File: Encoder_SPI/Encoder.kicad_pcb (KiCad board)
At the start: 2 copper layers, 21 x 17 mm, 11 parts, among them J1 Conn_01x06, J2 PWM, U1 AS5048A

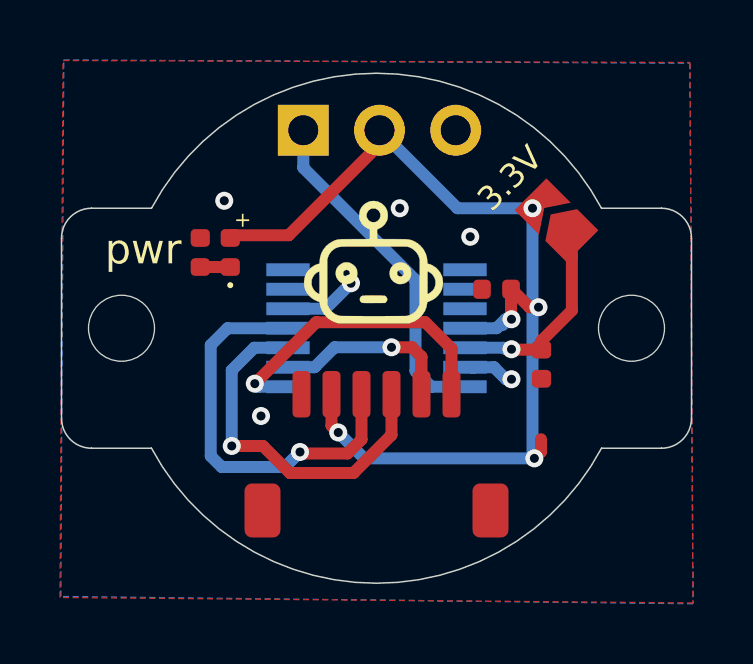
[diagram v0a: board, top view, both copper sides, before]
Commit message: Encoder_SPI update for new assembly order
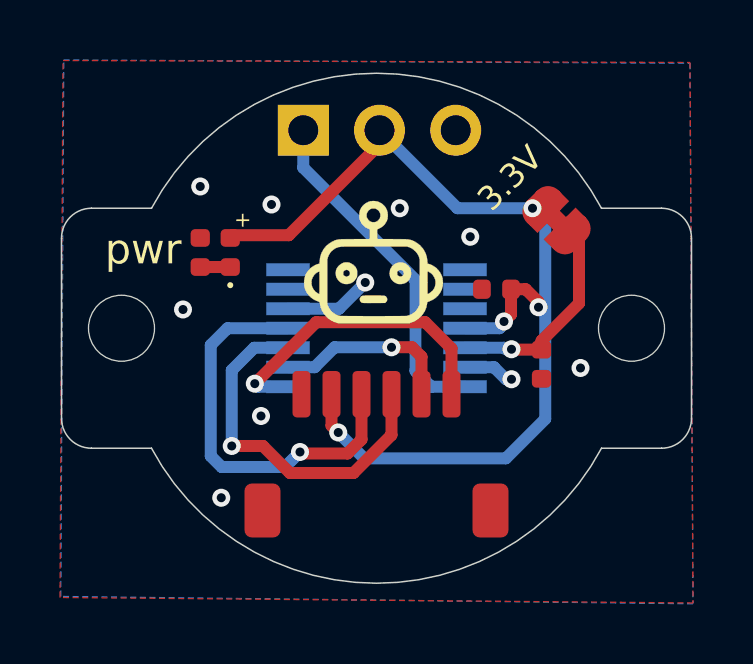
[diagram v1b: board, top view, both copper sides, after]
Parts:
- J1: value Conn_01x06 -> JST_SH_SM06B-SRSS-TB_1x06-1MP
- JP1: footprint Jumper:SolderJumper-2_P1.3mm_Open_TrianglePad1.0x1.5mm -> Jumper:SolderJumper-2_P1.3mm_Bridged_RoundedPad1.0x1.5mm
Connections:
- J1 pad MP: GND -> (no net)
- U1 pad 10: Net-(U1-Pad10) -> unconnected-(U1-Pad10)
- U1 pad 6: Net-(U1-Pad6) -> unconnected-(U1-Pad6)
- U1 pad 7: Net-(U1-Pad7) -> unconnected-(U1-Pad7)
- U1 pad 8: Net-(U1-Pad8) -> unconnected-(U1-Pad8)
- U1 pad 9: Net-(U1-Pad9) -> unconnected-(U1-Pad9)
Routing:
- net VCC: track 34.2 -> 33.0 mm, vias 5 -> 4
- net GND: track 4.45 -> 4.65 mm, vias 6 -> 10
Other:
- net class Default removed
- rule pad_to_mask_clearance: 0.05 -> 0
- board text added: "Measurements in mm"
- board text added: "d 2.2"
- board text added: "v1.1"
- board text added: "©2022"
- board text removed: "v1.0"
- board text removed: "©2021"
